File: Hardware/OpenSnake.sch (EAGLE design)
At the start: 30 parts, among them J2 AVR_SPI_PROG_3X2PTH, Q1 16MHZ, U1 ATMEGA328P, U2 317

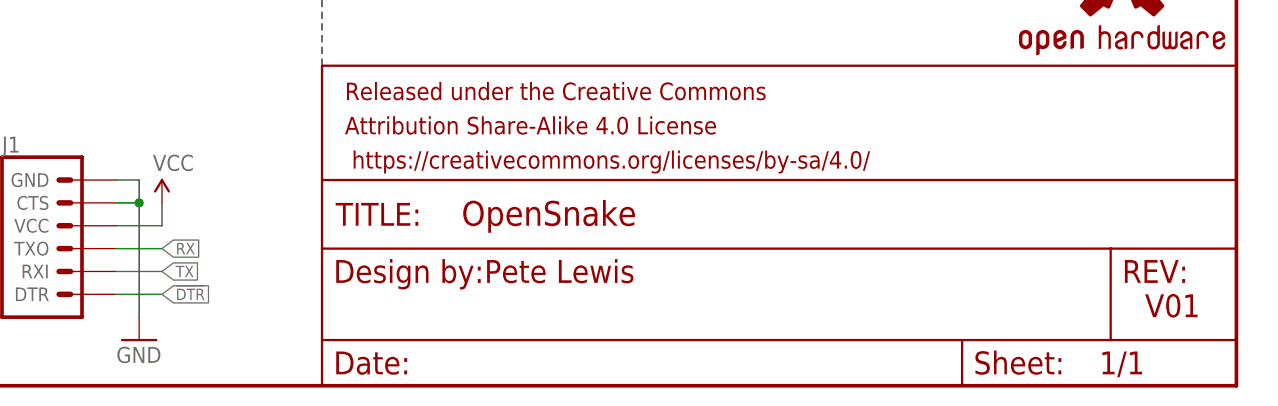
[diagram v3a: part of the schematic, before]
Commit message: Corrected RX/TX to 6-pin Serial programming header
I had these swapped on the header. Classic rookie mistake :)

-Swapped RX/TX on the serial header
-bumped version to v10 in sch and brd copper
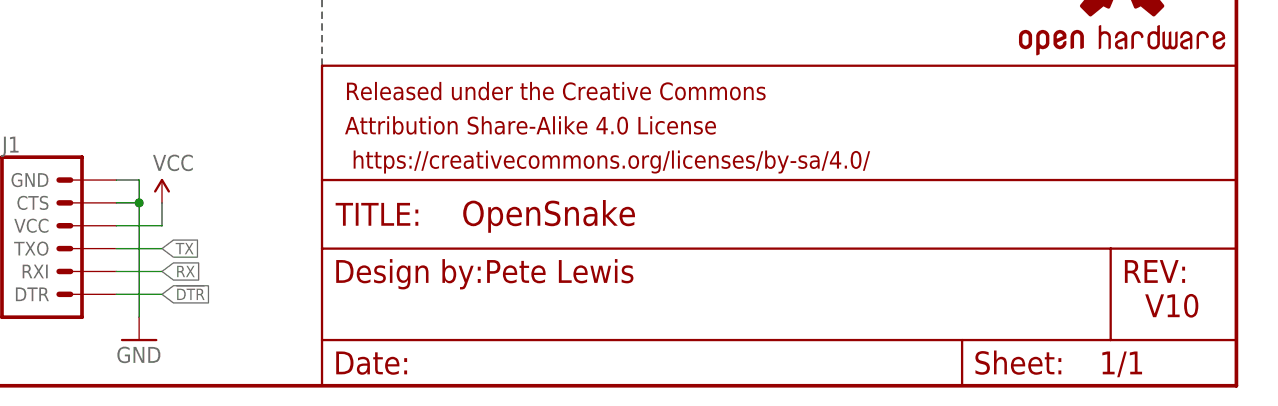
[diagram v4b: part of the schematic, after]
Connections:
- net RX: now also J1.RXI; no longer J1.TXO
- net TX: now also J1.TXO; no longer J1.RXI
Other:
- note added: "V10"
- note removed: "V01"
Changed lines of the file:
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@@
 <sheet>
 <plain>
-<text x="238.76" y="7.62" size="2.54" layer="94">V01</text>
+<text x="238.76" y="7.62" size="2.54" layer="94">V10</text>
 <text x="165.354" y="11.43" size="2.54" layer="94">Pete Lewis</text>
 <text x="2.54" y="177.8" size="2.54" layer="97">Power Circuit:</text>
@@
 <pinref part="GND7" gate="1" pin="GND"/>
 <wire x1="60.96" y1="17.78" x2="60.96" y2="20.32" width="0.1524" layer="91"/>
-</segment>
-<segment>
-<pinref part="J1" gate="G$1" pin="GND"/>
-<wire x1="124.46" y1="22.86" x2="127" y2="22.86" width="0.1524" layer="91"/>
-<wire x1="127" y1="22.86" x2="127" y2="20.32" width="0.1524" layer="91"/>
-<pinref part="J1" gate="G$1" pin="CTS"/>
-<wire x1="127" y1="20.32" x2="127" y2="7.62" width="0.1524" layer="91"/>
-<wire x1="124.46" y1="20.32" x2="127" y2="20.32" width="0.1524" layer="91"/>
-<junction x="127" y="20.32"/>
-<pinref part="GND9" gate="1" pin="GND"/>
 </segment>
 <segment>
@@
 <pinref part="GND12" gate="1" pin="GND"/>
 </segment>
+<segment>
+<pinref part="J1" gate="G$1" pin="GND"/>
+<wire x1="124.46" y1="22.86" x2="127" y2="22.86" width="0.1524" layer="91"/>
+<wire x1="127" y1="22.86" x2="127" y2="20.32" width="0.1524" layer="91"/>
+<pinref part="J1" gate="G$1" pin="CTS"/>
+<wire x1="124.46" y1="20.32" x2="127" y2="20.32" width="0.1524" layer="91"/>
+<pinref part="GND9" gate="1" pin="GND"/>
+<wire x1="127" y1="20.32" x2="127" y2="7.62" width="0.1524" layer="91"/>
+<junction x="127" y="20.32"/>
+</segment>
 </net>
 <net name="SCK" class="0">
@@
 </segment>
 <segment>
-<pinref part="J1" gate="G$1" pin="TXO"/>
-<wire x1="124.46" y1="15.24" x2="129.54" y2="15.24" width="0.1524" layer="91"/>
-<label x="129.54" y="15.24" size="1.27" layer="95" xref="yes"/>
+<pinref part="J1" gate="G$1" pin="RXI"/>
+<wire x1="124.46" y1="12.7" x2="129.54" y2="12.7" width="0.1524" layer="91"/>
+<label x="129.54" y="12.7" size="1.27" layer="95" xref="yes"/>
 </segment>
 </net>
@@
 </segment>
 <segment>
-<pinref part="J1" gate="G$1" pin="RXI"/>
-<wire x1="124.46" y1="12.7" x2="129.54" y2="12.7" width="0.1524" layer="91"/>
-<label x="129.54" y="12.7" size="1.27" layer="95" xref="yes"/>
-</segment>
-</net>
+<pinref part="J1" gate="G$1" pin="TXO"/>
+<wire x1="124.46" y1="15.24" x2="129.54" y2="15.24" width="0.1524" layer="91"/>
+<label x="129.54" y="15.24" size="1.27" layer="95" xref="yes"/>
+</segment>
+</net>

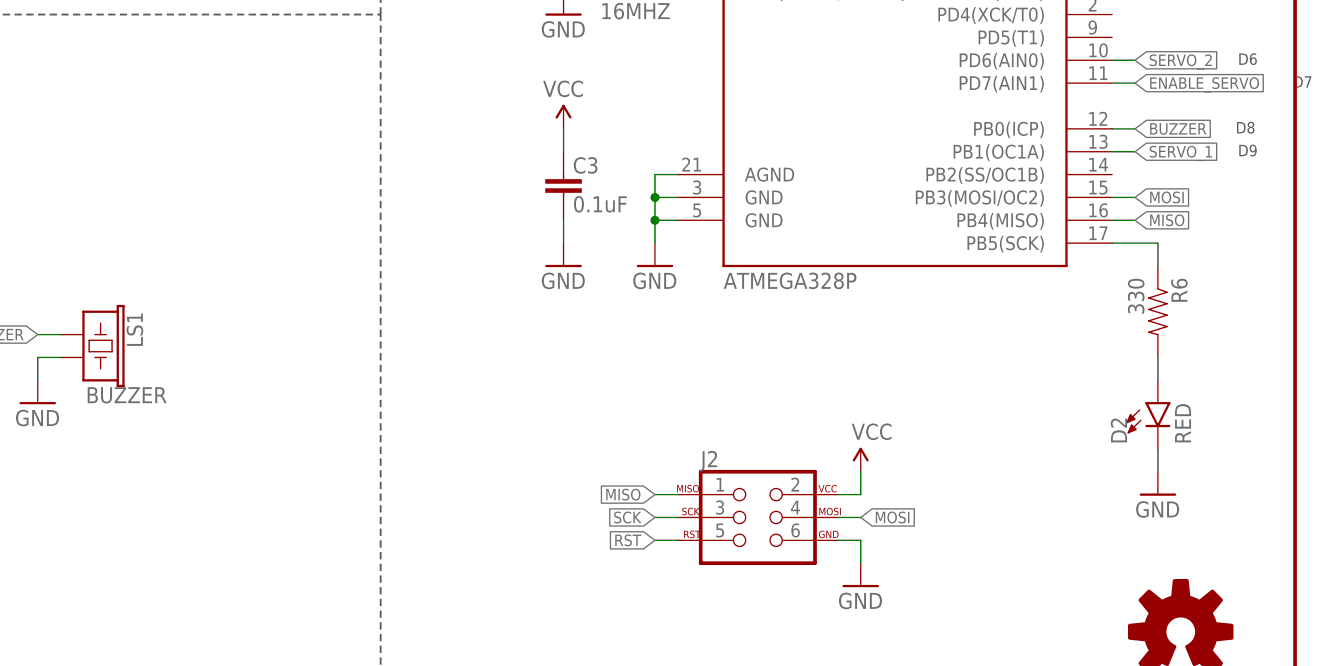
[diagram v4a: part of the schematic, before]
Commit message: final changes to v10
-added green LED
-added silk labels for servo ports
-Panelized and cammed
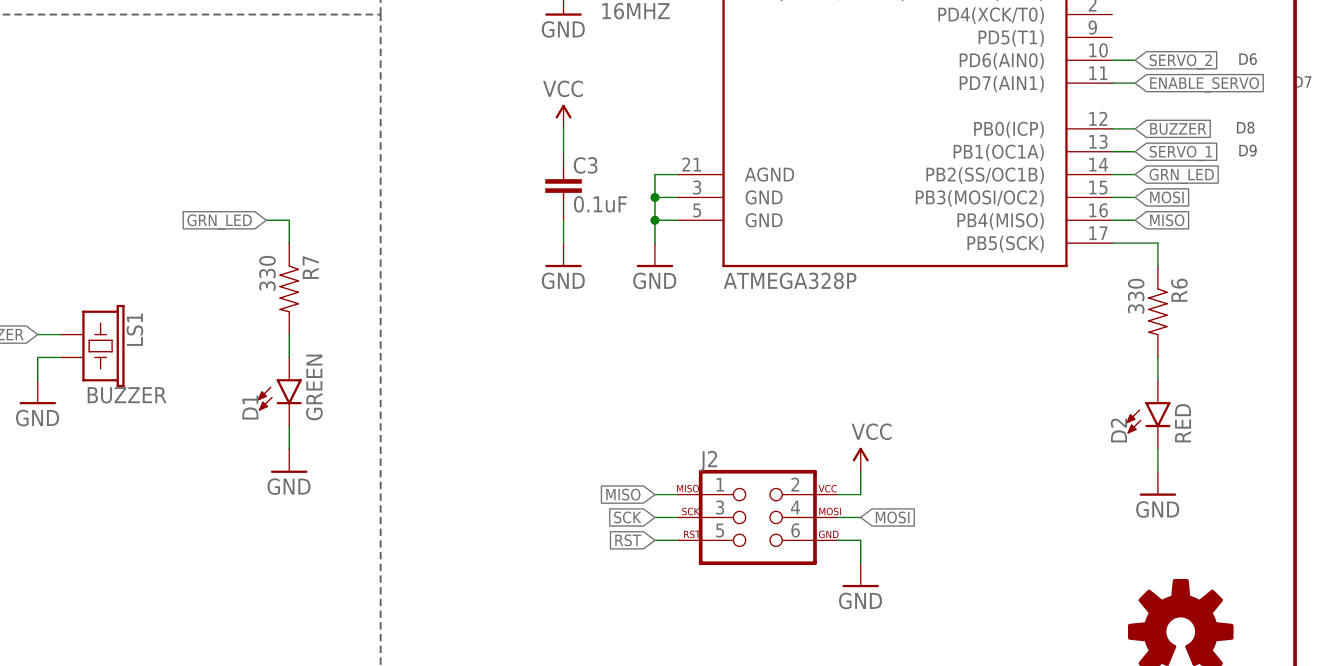
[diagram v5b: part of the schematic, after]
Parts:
- added D1: GREEN, SparkFun-LED:LED5MM
- added R7: 330, SparkFun-Resistors:330OHM1/10W1%(0603)
- D2: device SparkFun-LED:LED10MM -> SparkFun-LED:LED5MM
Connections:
- new net GRN_LED: R7.1, U1.PB2(SS/OC1B)
- new net N$10: D1.A, R7.2
- net GND: now also D1.C

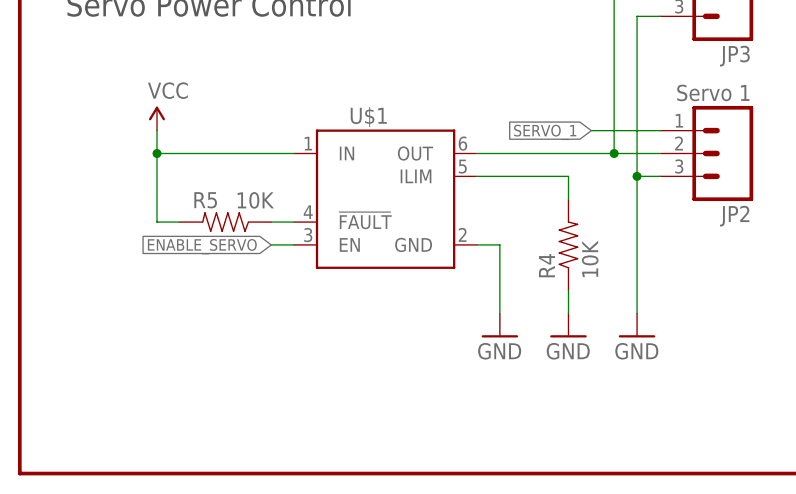
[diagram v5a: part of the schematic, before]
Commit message: assembly sheet optimization
-just positioning names and values so they print nicely
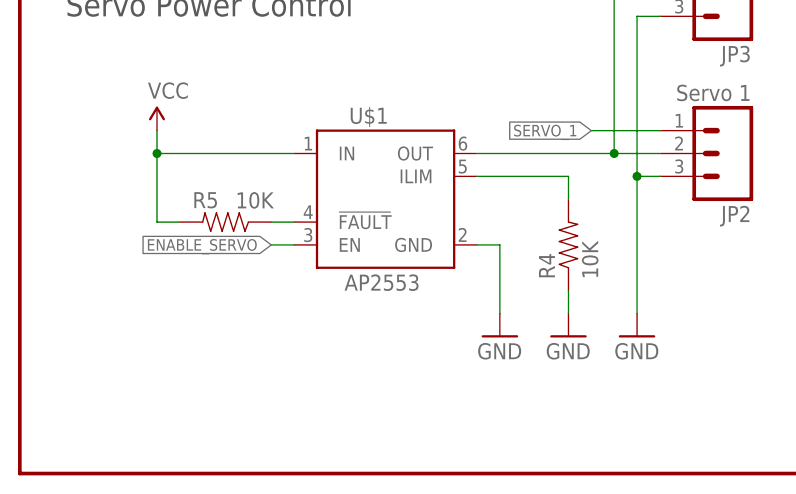
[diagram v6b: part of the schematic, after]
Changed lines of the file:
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@@
 <?xml version="1.0" encoding="utf-8"?>
 <!DOCTYPE eagle SYSTEM "eagle.dtd">
-<eagle version="9.5.2">
+<eagle version="9.6.2">
 <drawing>
 <settings>
@@
 <grid distance="0.1" unitdist="inch" unit="inch" style="lines" multiple="1" display="no" altdistance="0.01" altunitdist="inch" altunit="inch"/>
 <layers>
-<layer number="1" name="Top" color="4" fill="1" visible="yes" active="no"/>
-<layer number="2" name="Route2" color="1" fill="3" visible="yes" active="no"/>
-<layer number="3" name="Route3" color="4" fill="3" visible="yes" active="no"/>
-<layer number="4" name="Route4" color="1" fill="4" visible="yes" active="no"/>
-<layer number="5" name="Route5" color="4" fill="4" visible="yes" active="no"/>
-<layer number="6" name="Route6" color="1" fill="8" visible="yes" active="no"/>
-<layer number="7" name="Route7" color="4" fill="8" visible="yes" active="no"/>
-<layer number="8" name="Route8" color="1" fill="2" visible="yes" active="no"/>
-<layer number="9" name="Route9" color="4" fill="2" visible="yes" active="no"/>
-<layer number="10" name="Route10" color="1" fill="7" visible="yes" active="no"/>
-<layer number="11" name="Route11" color="4" fill="7" visible="yes" active="no"/>
-<layer number="12" name="Route12" color="1" fill="5" visible="yes" active="no"/>
-<layer number="13" name="Route13" color="4" fill="5" visible="yes" active="no"/>
-<layer number="14" name="Route14" color="1" fill="6" visible="yes" active="no"/>
-<layer number="15" name="Route15" color="4" fill="6" visible="yes" active="no"/>
-<layer number="16" name="Bottom" color="1" fill="1" visible="yes" active="no"/>
-<layer number="17" name="Pads" color="2" fill="1" visible="yes" active="no"/>
-<layer number="18" name="Vias" color="2" fill="1" visible="yes" active="no"/>
-<layer number="19" name="Unrouted" color="6" fill="1" visible="yes" active="no"/>
-<layer number="20" name="Dimension" color="24" fill="1" visible="yes" active="no"/>
-<layer number="21" name="tPlace" color="16" fill="1" visible="yes" active="no"/>
-<layer number="22" name="bPlace" color="14" fill="1" visible="yes" active="no"/>
-<layer number="23" name="tOrigins" color="15" fill="1" visible="yes" active="no"/>
-<layer number="24" name="bOrigins" color="15" fill="1" visible="yes" active="no"/>
-<layer number="25" name="tNames" color="7" fill="1" visible="yes" active="no"/>
-<layer number="26" name="bNames" color="7" fill="1" visible="yes" active="no"/>
-<layer number="27" name="tValues" color="7" fill="1" visible="yes" active="no"/>
-<layer number="28" name="bValues" color="7" fill="1" visible="yes" active="no"/>
+<layer number="1" name="Top" color="4" fill="1" visible="no" active="no"/>
+<layer number="2" name="Route2" color="1" fill="3" visible="no" active="no"/>
+<layer number="3" name="Route3" color="4" fill="3" visible="no" active="no"/>
+<layer number="4" name="Route4" color="1" fill="4" visible="no" active="no"/>
+<layer number="5" name="Route5" color="4" fill="4" visible="no" active="no"/>
+<layer number="6" name="Route6" color="1" fill="8" visible="no" active="no"/>
+<layer number="7" name="Route7" color="4" fill="8" visible="no" active="no"/>
+<layer number="8" name="Route8" color="1" fill="2" visible="no" active="no"/>
+<layer number="9" name="Route9" color="4" fill="2" visible="no" active="no"/>
+<layer number="10" name="Route10" color="1" fill="7" visible="no" active="no"/>
+<layer number="11" name="Route11" color="4" fill="7" visible="no" active="no"/>
+<layer number="12" name="Route12" color="1" fill="5" visible="no" active="no"/>
+<layer number="13" name="Route13" color="4" fill="5" visible="no" active="no"/>
+<layer number="14" name="Route14" color="1" fill="6" visible="no" active="no"/>
+<layer number="15" name="Route15" color="4" fill="6" visible="no" active="no"/>
+<layer number="16" name="Bottom" color="1" fill="1" visible="no" active="no"/>
+<layer number="17" name="Pads" color="2" fill="1" visible="no" active="no"/>
+<layer number="18" name="Vias" color="2" fill="1" visible="no" active="no"/>
+<layer number="19" name="Unrouted" color="6" fill="1" visible="no" active="no"/>
+<layer number="20" name="Dimension" color="24" fill="1" visible="no" active="no"/>
+<layer number="21" name="tPlace" color="16" fill="1" visible="no" active="no"/>
+<layer number="22" name="bPlace" color="14" fill="1" visible="no" active="no"/>
+<layer number="23" name="tOrigins" color="15" fill="1" visible="no" active="no"/>
+<layer number="24" name="bOrigins" color="15" fill="1" visible="no" active="no"/>
+<layer number="25" name="tNames" color="7" fill="1" visible="no" active="no"/>
+<layer number="26" name="bNames" color="7" fill="1" visible="no" active="no"/>
+<layer number="27" name="tValues" color="7" fill="1" visible="no" active="no"/>
+<layer number="28" name="bValues" color="7" fill="1" visible="no" active="no"/>
 <layer number="29" name="tStop" color="7" fill="3" visible="no" active="no"/>
 <layer number="30" name="bStop" color="7" fill="6" visible="no" active="no"/>
@@
 <layer number="35" name="tGlue" color="7" fill="4" visible="no" active="no"/>
 <layer number="36" name="bGlue" color="7" fill="5" visible="no" active="no"/>
-<layer number="37" name="tTest" color="7" fill="1" visible="yes" active="no"/>
-<layer number="38" name="bTest" color="7" fill="1" visible="yes" active="no"/>
+<layer number="37" name="tTest" color="7" fill="1" visible="no" active="no"/>
+<layer number="38" name="bTest" color="7" fill="1" visible="no" active="no"/>
 <layer number="39" name="tKeepout" color="4" fill="11" visible="no" active="no"/>
 <layer number="40" name="bKeepout" color="1" fill="11" visible="no" active="no"/>
@@
 <layer number="44" name="Drills" color="7" fill="1" visible="no" active="no"/>
 <layer number="45" name="Holes" color="7" fill="1" visible="no" active="no"/>
-<layer number="46" name="Milling" color="3" fill="1" visible="yes" active="no"/>
-<layer number="47" name="Measures" color="7" fill="1" visible="yes" active="no"/>
-<layer number="48" name="Document" color="7" fill="1" visible="yes" active="no"/>
-<layer number="49" name="Reference" color="13" fill="1" visible="yes" active="no"/>
-<layer number="50" name="dxf" color="7" fill="1" visible="yes" active="no"/>
-<layer number="51" name="tDocu" color="6" fill="1" visible="yes" active="no"/>
-<layer number="52" name="bDocu" color="7" fill="1" visible="yes" active="no"/>
-<layer number="53" name="tGND_GNDA" color="7" fill="9" visible="yes" active="no"/>
-<layer number="54" name="bGND_GNDA" color="1" fill="9" visible="yes" active="no"/>
-<layer number="56" name="wert" color="7" fill="1" visible="yes" active="no"/>
-<layer number="57" name="tCAD" color="7" fill="1" visible="yes" active="no"/>
-<layer number="59" name="tCarbon" color="7" fill="1" visible="yes" active="no"/>
-<layer number="60" name="bCarbon" color="7" fill="1" visible="yes" active="no"/>
+<layer number="46" name="Milling" color="3" fill="1" visible="no" active="no"/>
+<layer number="47" name="Measures" color="7" fill="1" visible="no" active="no"/>
+<layer number="48" name="Document" color="7" fill="1" visible="no" active="no"/>
+<layer number="49" name="Reference" color="13" fill="1" visible="no" active="no"/>
+<layer number="50" name="dxf" color="7" fill="1" visible="no" active="no"/>
+<layer number="51" name="tDocu" color="6" fill="1" visible="no" active="no"/>
+<layer number="52" name="bDocu" color="7" fill="1" visible="no" active="no"/>
+<layer number="53" name="tGND_GNDA" color="7" fill="9" visible="no" active="no"/>
+<layer number="54" name="bGND_GNDA" color="1" fill="9" visible="no" active="no"/>
+<layer number="56" name="wert" color="7" fill="1" visible="no" active="no"/>
+<layer number="57" name="tCAD" color="7" fill="1" visible="no" active="no"/>
+<layer number="59" name="tCarbon" color="7" fill="1" visible="no" active="no"/>
+<layer number="60" name="bCarbon" color="7" fill="1" visible="no" active="no"/>
 <layer number="88" name="SimResults" color="9" fill="1" visible="yes" active="yes"/>
 <layer number="89" name="SimProbes" color="9" fill="1" visible="yes" active="yes"/>
@@
 <part name="R3" library="SparkFun-Resistors" deviceset="330OHM1/10W1%(0603)" device="" value="240"/>
 <part name="GND2" library="SparkFun" deviceset="GND" device=""/>
-<part name="U$1" library="snake" deviceset="AP2553" device="" value=""/>
+<part name="U$1" library="snake" deviceset="AP2553" device="" value="AP2553"/>
 <part name="GND3" library="SparkFun" deviceset="GND" device=""/>
 <part name="R4" library="SparkFun-Resistors" deviceset="10KOHM-1/10W-1%(0603)" device="0603" value="10K"/>
